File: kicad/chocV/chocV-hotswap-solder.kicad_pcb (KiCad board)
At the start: 2 copper layers, 215 x 78.8 mm, 84 parts, among them SW1 SW_Push, SW10 SW_Push, SW11 SW_Push, SW12 SW_Push, SW13 SW_Push, SW14 SW_Push, SW15 SW_Push, SW16 SW_Push, SW17 SW_Push, SW18 SW_Push, SW19 SW_Push, SW2 SW_Push, SW20 SW_Push, SW21 SW_Push, SW22 SW_Push, SW23 SW_Push, SW24 SW_Push, SW25 SW_Push, SW26 SW_Push, SW27 SW_Push, SW28 SW_Push, SW29 SW_Push, SW3 SW_Push, SW30 SW_Push, SW31 SW_Push, SW32 SW_Push, SW33 SW_Push, SW34 SW_Push, SW35 SW_Push, SW36 SW_Push, SW37 Reset Switch, SW4 SW_Push, SW5 SW_Push, SW6 SW_Push, SW7 SW_Push, SW8 SW_Push, SW9 SW_Push, U1 Pro-Micro

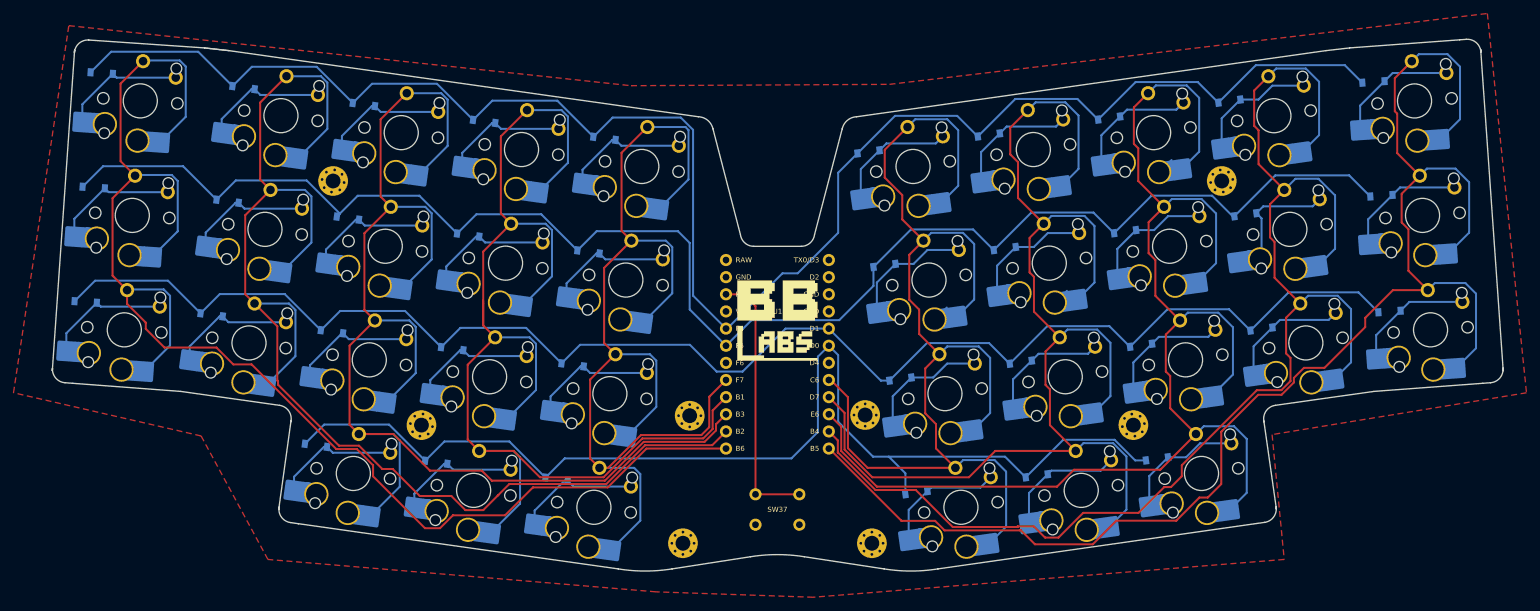
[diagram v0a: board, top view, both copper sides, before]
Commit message: add rounded tracks, update readme
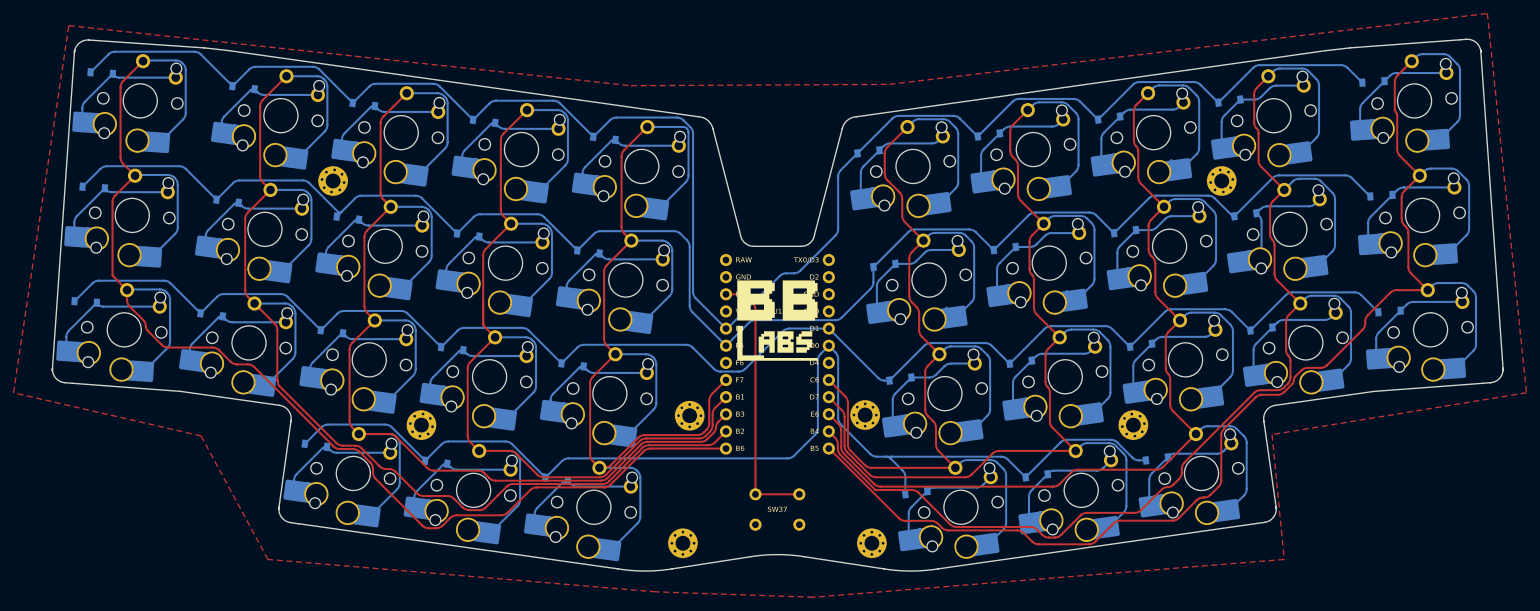
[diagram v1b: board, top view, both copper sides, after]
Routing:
- net col9: track 199.9 -> 197.2 mm
- net col10: track 216.7 -> 214.0 mm
- net col8: track 205.5 -> 203.3 mm
- net col7: track 187.4 -> 185.3 mm
- net col6: track 170.8 -> 168.7 mm
- net col1: track 208.2 -> 206.2 mm
- net col3: track 197.1 -> 195.3 mm
- net col2: track 189.2 -> 187.4 mm
- net row1: track 260.6 -> 259.0 mm
- net col5: track 162.4 -> 160.9 mm
- net row3: track 229.5 -> 228.1 mm
- net col4: track 184.1 -> 182.7 mm
- net row2: track 239.7 -> 238.9 mm
